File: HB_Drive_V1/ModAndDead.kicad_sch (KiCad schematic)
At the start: 31 parts, among them J401 Conn_01x03, U401 LM311, U402 74LS08, U403 74AHC1G125, U404 74AHC1GU04, U405 74AHC1GU04, U406 74AHC1G125

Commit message: restores v2 to condtion as ordered!
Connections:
- net GND: now also U403.1, U406.1
- net D_Cmd renamed Duty
- no-connect marks 6 -> 4
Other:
- note added: "H_Raw"
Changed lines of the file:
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@@
 		)
 	)
+	(text "H_Raw"
+		(exclude_from_sim no)
+		(at 206.248 111.76 0)
+		(effects
+			(font
+				(size 1.27 1.27)
+			)
+			(justify left)
+		)
+	)
+	(text "H_Raw"
+		(exclude_from_sim no)
+		(at 207.01 124.714 0)
+		(effects
+			(font
+				(size 1.27 1.27)
+			)
+			(justify left)
+		)
+	)
 	(text "H_CMD Inversion"
 		(exclude_from_sim no)
@@
 	)
 	(no_connect
-		(at 284.48 96.52)
-	)
-	(no_connect
 		(at 96.52 105.41)
 	)
@@
 		(at 93.98 105.41)
 	)
-	(no_connect
-		(at 189.23 93.98)
-	)
 	(wire
 		(pts
@@
 		)
 	)
+	(polyline
+		(pts
+			(xy 207.01 123.19) (xy 213.36 123.19)
+		)
+		(stroke
+			(width 0)
+			(type default)
+		)
+	)
 	(wire
 		(pts
@@
 	(wire
 		(pts
+			(xy 284.48 96.52) (xy 297.18 96.52)
+		)
+		(stroke
+			(width 0)
+			(type default)
+		)
+	)
+	(wire
+		(pts
 			(xy 177.8 92.71) (xy 177.8 93.98)
 		)
@@
 	(wire
 		(pts
+			(xy 189.23 93.98) (xy 200.66 93.98)
+		)
+		(stroke
+			(width 0)
+			(type default)
+		)
+	)
+	(wire
+		(pts
 			(xy 166.37 119.38) (xy 170.18 119.38)
 		)
@@
 		)
 	)
-	(hierarchical_label "D_Cmd"
+	(hierarchical_label "Duty"
 		(shape input)
 		(at 59.69 110.49 180)
@@
 		(dnp no)
 		(property "Reference" "R401"
-			(at 67.31 112.776 90)
+			(at 67.564 103.886 90)
 			(show_name no)
 			(do_not_autoplace no)
@@
 	)
 	(symbol
+		(lib_id "power:GND")
+		(at 297.18 96.52 0)
+		(mirror y)
+		(unit 1)
+		(body_style 1)
+		(exclude_from_sim no)
+		(in_bom yes)
+		(on_board yes)
+		(in_pos_files yes)
+		(dnp no)
+		(property "Reference" "#PWR0426"
+			(at 297.18 102.87 0)
+			(hide yes)
+			(show_name no)
+			(do_not_autoplace no)
+			(effects
+				(font
+					(size 1.27 1.27)
+				)
+			)
+		)
+		(property "Value" "GND"
+			(at 300.736 99.06 0)
+			(show_name no)
+			(do_not_autoplace no)
+			(effects
+				(font
+					(size 1.27 1.27)
+				)
+			)
+		)
+		(property "Footprint" ""
+			(at 297.18 96.52 0)
+			(hide yes)
+			(show_name no)
+			(do_not_autoplace no)
+			(effects
+				(font
+					(size 1.27 1.27)
+				)
+			)
+		)
+		(property "Datasheet" ""
+			(at 297.18 96.52 0)
+			(hide yes)
+			(show_name no)
+			(do_not_autoplace no)
+			(effects
+				(font
+					(size 1.27 1.27)
+				)
+			)
+		)
+		(property "Description" "Power symbol creates a global label with name \"GND\" , ground"
+			(at 297.18 96.52 0)
+			(hide yes)
+			(show_name no)
+			(do_not_autoplace no)
+			(effects
+				(font
+					(size 1.27 1.27)
+				)
+			)
+		)
+		(pin "1"
+		)
+		(instances
+			(project "HB_Drive_V1"
+				(path "/a9b54c89-4c8e-4c90-8a0d-ec2009e369b7/28e2d9d3-ebce-4623-8c7e-52f93025d826/97cfd595-263d-4fe9-9bac-f56dcdbd61fb"
+					(reference "#PWR0426")
+					(unit 1)
+				)
+			)
+		)
+	)
+	(symbol
 		(lib_id "Device:C")
 		(at 269.24 121.92 270)
@@
 		(dnp no)
 		(property "Reference" "R402"
-			(at 67.056 118.364 90)
+			(at 67.818 106.172 90)
 			(show_name no)
 			(do_not_autoplace no)
@@
 		(property "Value" "1KΩ"
 			(at 67.31 118.11 90)
+			(hide yes)
 			(show_name no)
 			(do_not_autoplace no)
@@
 					(unit 1)
 				)
+			)
+		)
+	)
+	(symbol
+		(lib_id "power:GND")
+		(at 200.66 93.98 0)
+		(mirror y)
+		(unit 1)
+		(body_style 1)
+		(exclude_from_sim no)
+		(in_bom yes)
+		(on_board yes)
+		(in_pos_files yes)
+		(dnp no)
+		(property "Reference" "#PWR0425"
+			(at 200.66 100.33 0)
+			(hide yes)
+			(show_name no)
+			(do_not_autoplace no)
+			(effects
+				(font
+					(size 1.27 1.27)
+				)
+			)
+		)
+		(property "Value" "GND"
+			(at 204.216 96.52 0)
+			(show_name no)
+			(do_not_autoplace no)
+			(effects
+				(font
+					(size 1.27 1.27)
+				)
+			)
+		)
+		(property "Footprint" ""
+			(at 200.66 93.98 0)
+			(hide yes)
+			(show_name no)
+			(do_not_autoplace no)
+			(effects
+				(font
+					(size 1.27 1.27)
+				)
+			)
+		)
+		(property "Datasheet" ""
+			(at 200.66 93.98 0)
+			(hide yes)
+			(show_name no)
+			(do_not_autoplace no)
+			(effects
+				(font
+					(size 1.27 1.27)
+				)
+			)
+		)
+		(property "Description" "Power symbol creates a global label with name \"GND\" , ground"
+			(at 200.66 93.98 0)
+			(hide yes)
+			(show_name no)
+			(do_not_autoplace no)
+			(effects
+				(font
+					(size 1.27 1.27)
+				)
+			)
+		)
+		(pin "1"
+		)
+		(instances
+			(project "HB_Drive_V1"
+				(path "/a9b54c89-4c8e-4c90-8a0d-ec2009e369b7/28e2d9d3-ebce-4623-8c7e-52f93025d826/97cfd595-263d-4fe9-9bac-f56dcdbd61fb"
+					(reference "#PWR0425")
+					(unit 1)
+				)

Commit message: Brings everything up to latest copy on my computer
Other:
- company: (none) -> UW Madison, WEMPEC
- title: (none) -> HB Drive V3
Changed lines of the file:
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@@
 	(generator_version "10.0")
 	(paper "A3")
+	(title_block
+		(title "HB Drive V3")
+		(date "2026-09-08")
+		(company "UW Madison, WEMPEC")
+	)
 	(rectangle
 		(start 36.83 90.17)

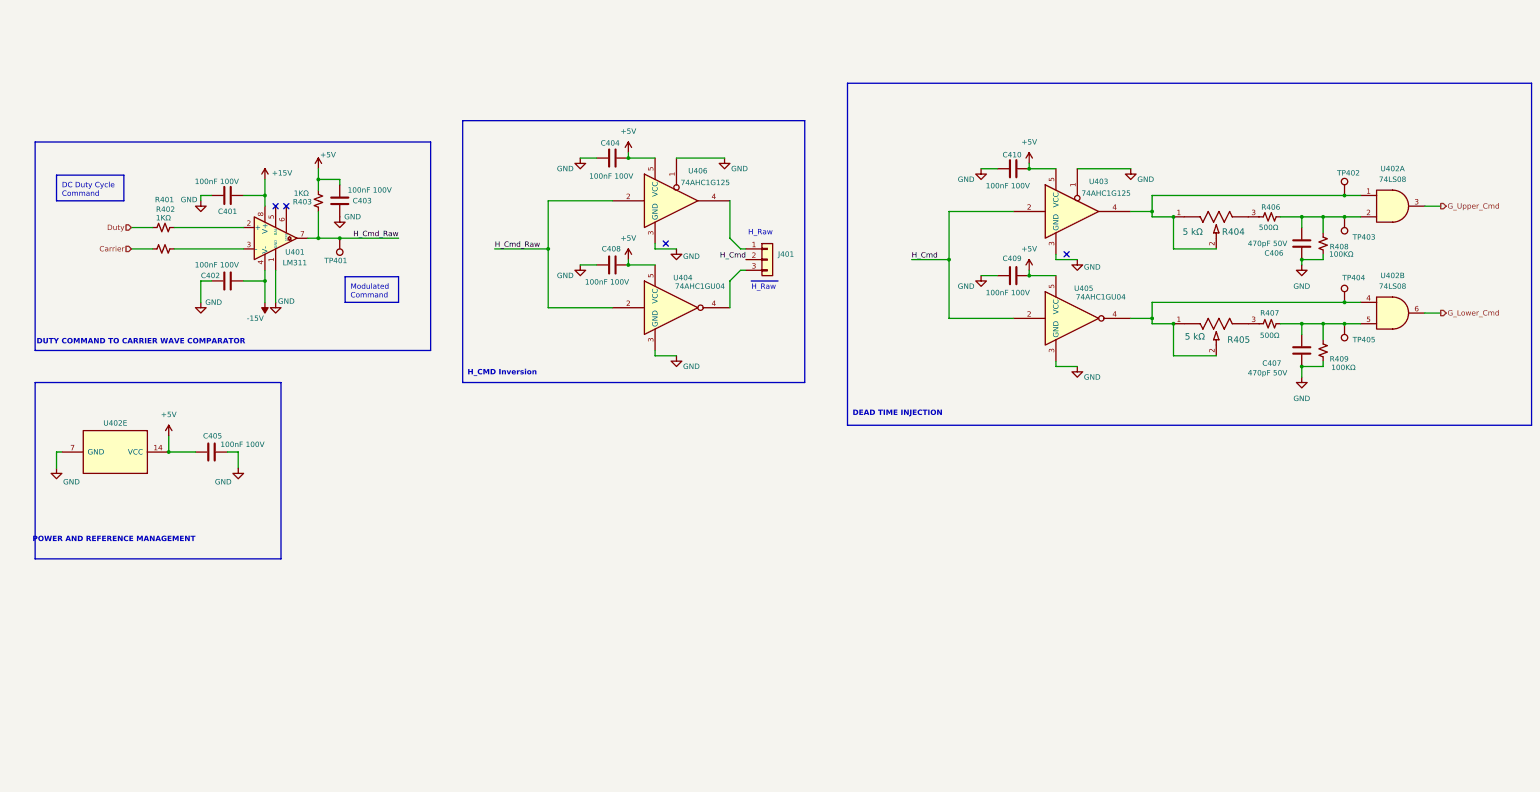
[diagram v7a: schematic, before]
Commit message: Makes annotation changes
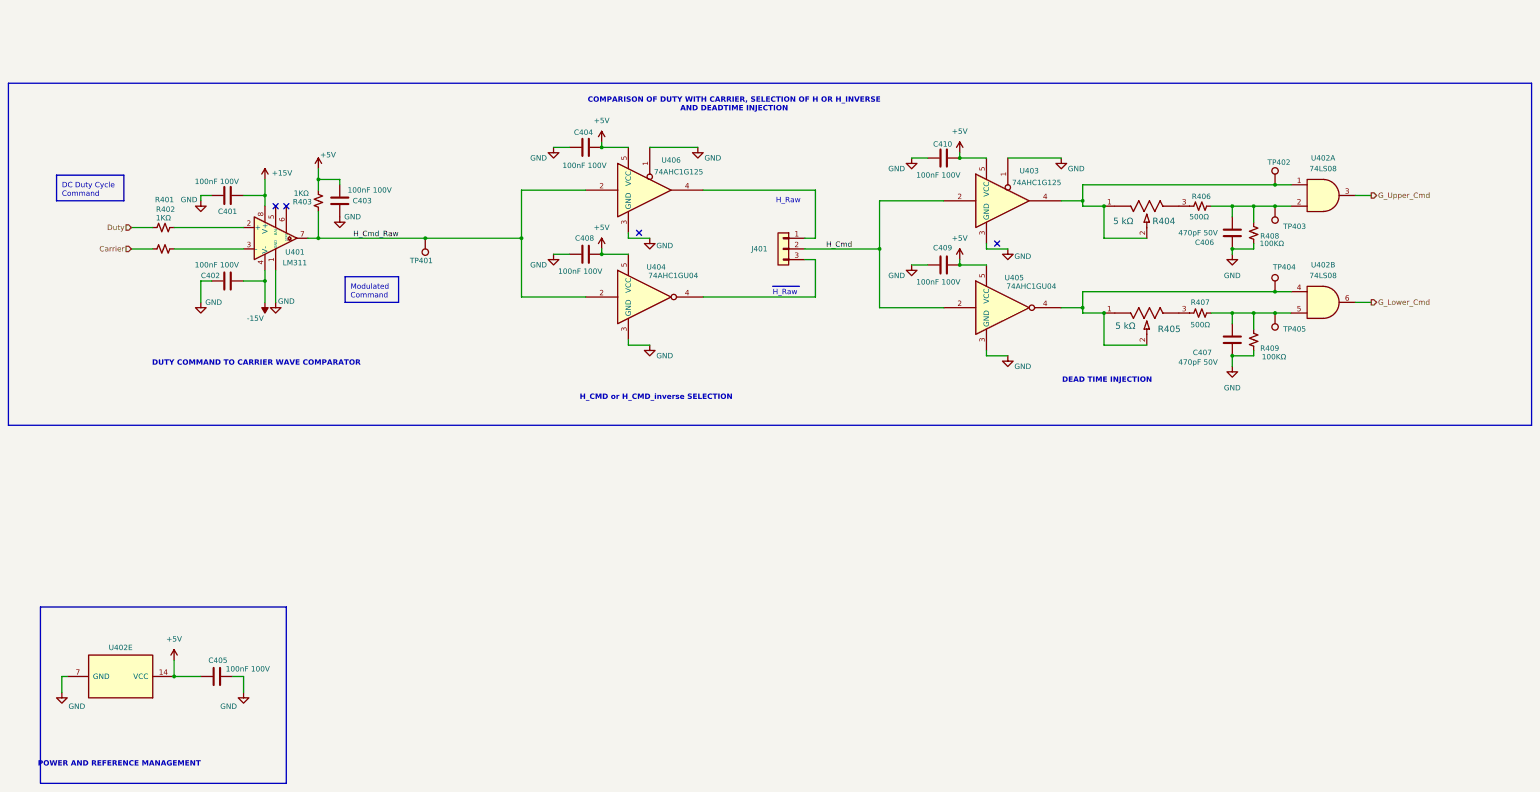
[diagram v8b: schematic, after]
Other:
- note added: "COMPARISON OF DUTY WITH CARRIER, SELECTION OF H OR H_INVERSE AND DEADTIME INJECTION"
- note added: "H_CMD or H_CMD_inverse SELECTION"
- note removed: "H_CMD Inversion"
- moved on the sheet: C404, C405, C406, C407, C408, C409, C410, J401, R404, R405, R406, R407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
